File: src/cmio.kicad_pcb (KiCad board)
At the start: 2 copper layers, 78.7 x 29.2 mm, 37 parts, among them J1 USB_POWER, J3 BANK0, J4 USB_OTG, J5 CM3Lite, J6 TVOUT, J7 BANK1, J8 Micro_SD_Card_TFP09_2_12B, SW1 Reset, U1 AP3417B, U2 AP3417B, U3 SP6203EM5-L-2-8/TR, U4 AP2401

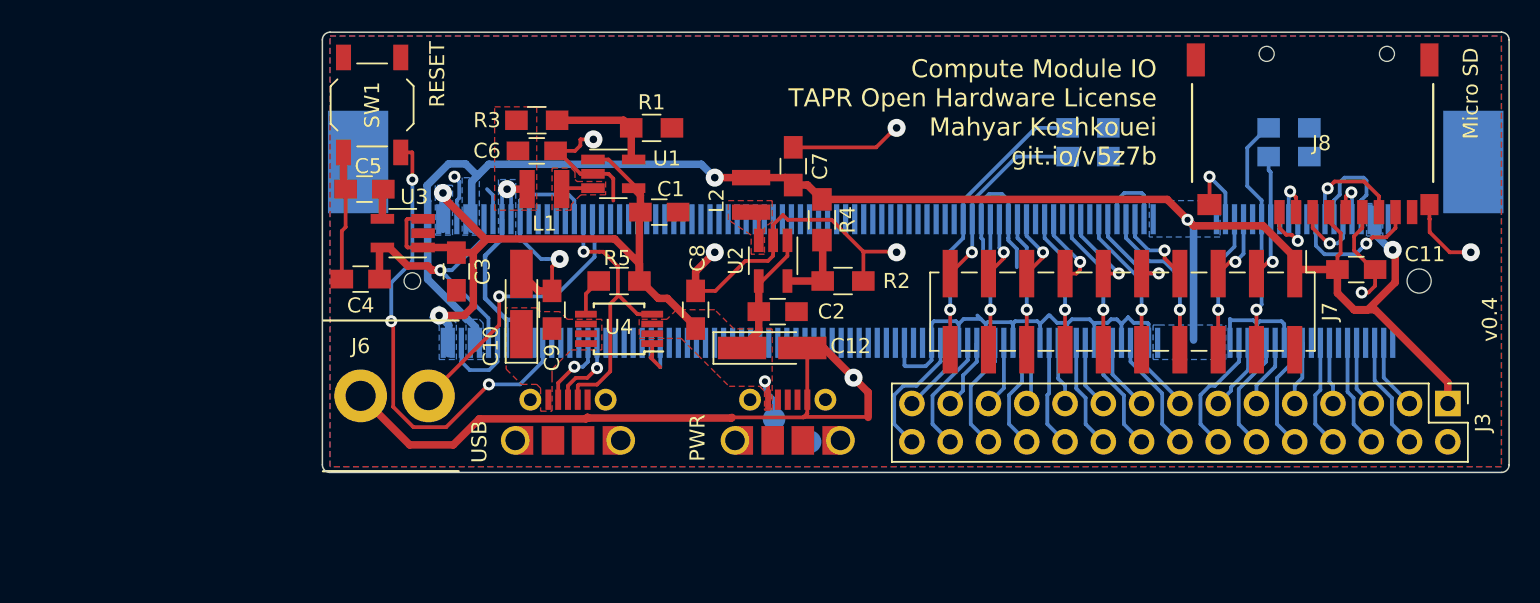
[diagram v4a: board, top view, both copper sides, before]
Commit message: Complete Routing
Signed-off-by: Mahyar Koshkouei <mahyar.koshkouei@gmail.com>
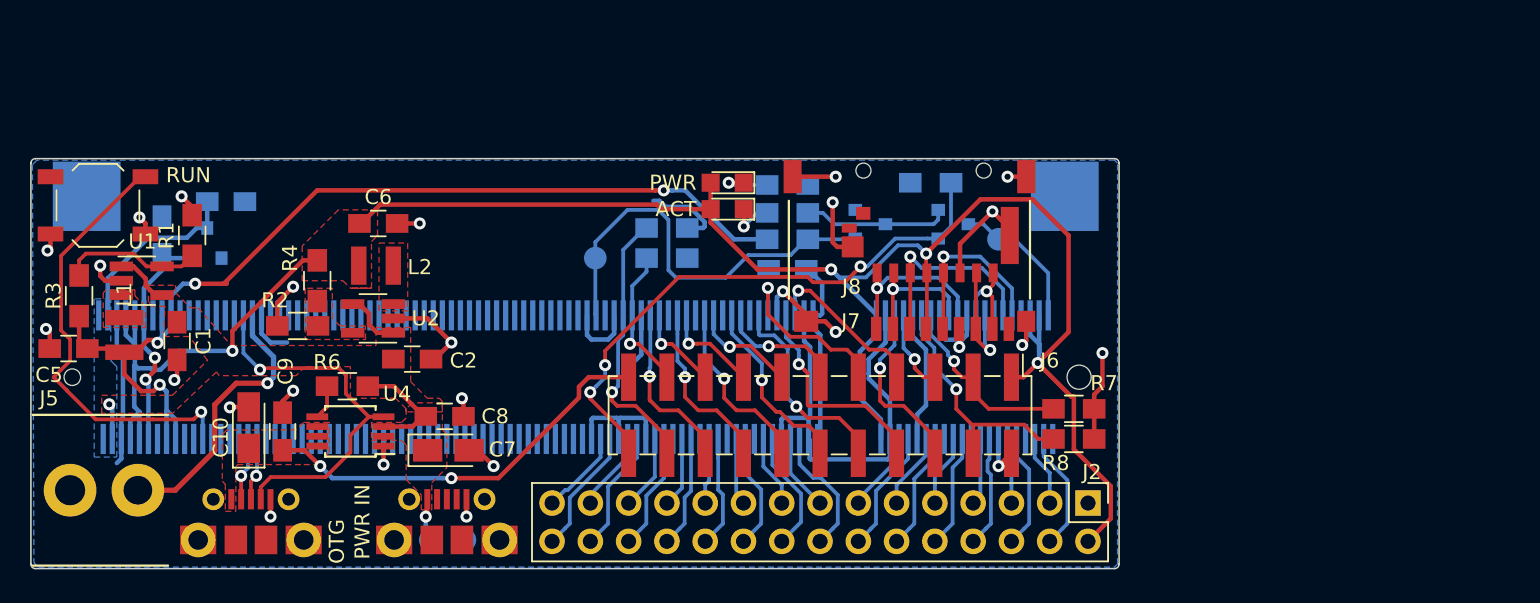
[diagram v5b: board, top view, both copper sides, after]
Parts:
- removed C12: 47uF, Capacitors_Tantalum_SMD:CP_Tantalum_Case-A_EIA-3216-18_Hand
- removed J1: USB_POWER, foot:Molex_Right_Angle_SMT_TypeB_MicroUSB_105017_CircularOnly
- removed J3: BANK0, Pin_Headers:Pin_Header_Straight_2x15_Pitch2.54mm
- removed SW1: Reset, Buttons_Switches_SMD:SW_SPST_TL3342
- added ACT: STATUS LED, LEDs:LED_0805, F.Cu at (131.0, 91.8)
- added J2: BANK0, Pin_Headers:Pin_Header_Straight_2x15_Pitch2.54mm, F.Cu at (154.9, 111.3)
- added OTG: USB_OTG, foot:Molex_Right_Angle_SMT_TypeB_MicroUSB_105017_CircularOnly_annular_fix, F.Cu at (99.4, 111.0)
- added PWR: PWR LED, LEDs:LED_0805, F.Cu at (131.0, 90.0)
- added PWR IN: USB_POWER, foot:Molex_Right_Angle_SMT_TypeB_MicroUSB_105017_CircularOnly_annular_fix, F.Cu at (112.4, 111.0)
- added Q1: 2N7002, TO_SOT_Packages_SMD:SOT-23, B.Cu at (146.0, 92.8)
- added Q2: 2N7002, TO_SOT_Packages_SMD:SOT-23, B.Cu at (140.5, 92.8)
- added R10: 100k, Resistors_SMD:R_0805_HandSoldering, B.Cu at (127.0, 93.0)
- added R11: 100k, Resistors_SMD:R_0805_HandSoldering, B.Cu at (135.0, 93.8)
- added R12: 100k, Resistors_SMD:R_0805_HandSoldering, B.Cu at (144.5, 90.0)
- added R13: 470R, Resistors_SMD:R_0805_HandSoldering, B.Cu at (135.0, 92.0)
- added RUN: Reset, Buttons_Switches_SMD:SW_SPST_TL3342, F.Cu at (89.2, 91.5)
- added TP3: TEST, Measurement_Points:Measurement_Point_Round-SMD-Pad_Small, B.Cu at (149.0, 93.8)
- added TP4: TEST, Measurement_Points:Measurement_Point_Round-SMD-Pad_Small, B.Cu at (122.2, 95.0)
- C10: footprint Capacitors_Tantalum_SMD:CP_Tantalum_Case-A_EIA-3216-18_Hand -> Capacitors_Tantalum_SMD:CP_Tantalum_Case-A_EIA-3216-18_Reflow
- C11: value 0.1uF -> 4.7uF; moved to B.Cu
- C3, C4: value 4.7uF -> 1uF; moved to B.Cu
- C5: value 10nF -> 4.7uF
- C7: value 4.7uF -> 47uF; footprint Capacitors_SMD:C_0805_HandSoldering -> Capacitors_Tantalum_SMD:CP_Tantalum_Case-A_EIA-3216-18_Reflow
- J4: value USB_OTG -> CM3Lite; footprint foot:Molex_Right_Angle_SMT_TypeB_MicroUSB_105017_CircularOnly -> foot:CM3_Socket_SODIMM_DDR1-2_TE_1473149_4_NoHole_NoEndSilkS; moved to B.Cu
- J5: value CM3Lite -> TVOUT; footprint foot:CM3_Socket_SODIMM_DDR1-2_TE_1612618_NoHole_NoEndSilkS -> foot:RCA_PHONO; moved to F.Cu
- J6: value TVOUT -> Conn_02x11_Odd_Even; footprint foot:RCA_PHONO -> Pin_Headers:Pin_Header_Straight_2x11_Pitch2.54mm_SMD
- J7: value BANK1 -> Micro_SD_Card_TFP09_2_12B; footprint Pin_Headers:Pin_Header_Straight_2x10_Pitch2.54mm_SMD -> foot:TFP09-2-12B
- J8: value Micro_SD_Card_TFP09_2_12B -> Micro_SD_Card_Molex_47219-2001; footprint foot:TFP09-2-12B -> foot:Molex_Micro_SD_47309-3751
- R5: value 10K -> 470R; moved to B.Cu
- R6: value 100K -> 10k; moved to F.Cu
- R7, R8: value 100K -> 100k; moved to F.Cu
- R9: value 100K -> 100k
- U3: value SP6203EM5-L-2-8/TR -> AP2138; footprint TO_SOT_Packages_SMD:SOT-23-5_HandSoldering -> TO_SOT_Packages_SMD:SOT-23; moved to B.Cu
- moved R6 64.3 mm to (105.8, 103.5), turned to 180 degrees
- moved J5 57.8 mm to (87.4, 110.4), turned to 0 degrees
- moved C11 37.7 mm to (135.0, 95.8), turned to 180 degrees
- moved R2 36.3 mm to (102.5, 99.5), turned to 180 degrees
- moved R4 33.7 mm to (103.8, 96.5)
- moved C1 33.1 mm to (94.5, 100.5), turned to 270 degrees
- moved J4 32.9 mm to (87.5, 102.9), turned to 180 degrees
- moved R3 32.5 mm to (88.0, 97.5), turned to 90 degrees
- moved U1 32.1 mm to (92.2, 96.5)
- moved R1 31.3 mm to (95.5, 93.5), turned to 90 degrees
- moved J6 30.5 mm to (137.2, 105.4), turned to 270 degrees
- moved C7 29.6 mm to (112.5, 107.8), turned to 0 degrees
- moved L1 29.5 mm to (91.0, 100.1), turned to 270 degrees
- moved R9 29.2 mm to (127.0, 95.0)
- moved U2 26.8 mm to (107.5, 99.0), turned to 180 degrees
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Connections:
- C10 pad 1: Net-(C10-Pad1) -> VBUS
- C4 pad 1: +2V8 -> +2V5
- C5 pad 1: GND -> +1V8
- C5 pad 2: Net-(C5-Pad2) -> GND
- C6 pad 1: +1V8 -> +3V3
- C7 pad 1: +3V3 -> +5V
- C9 pad 1: Net-(C10-Pad1) -> VBUS
- J4 pad 1: Net-(C10-Pad1) -> GND
- J4 pad 2: /D- -> EMMC_DISABLE_N
- J4 pad 3: /D+ -> /BCM_0
- J4 pad 4: OTGID -> +3V3
- J4 pad 5: GND -> /BCM_1
- J5 pad 1: GND -> /TV
- J5 pad 2: Net-(J5-Pad2) -> GND
- J6 pad 1: Net-(J5-Pad166) -> +3V3
- J7 pad 1: +3V3 -> DAT2
- J7 pad 10: /BCM_35 -> GND
- J7 pad 2: GND -> DAT3
- J7 pad 3: /BCM_28 -> CMD
- J7 pad 4: /BCM_29 -> +3V3
- J7 pad 5: /BCM_30 -> CLK
- J7 pad 6: /BCM_31 -> GND
- J7 pad 7: /BCM_32 -> DAT0
- J7 pad 8: /BCM_33 -> DAT1
- J7 pad 9: /BCM_34 -> Net-(J7-Pad9)
- J8 pad 9: Net-(J8-Pad9) -> GND
- R5 pad 1: +5V -> Net-(D1-Pad1)
- R5 pad 2: Net-(R5-Pad2) -> GND
- R6 pad 1: /BCM_28 -> +5V
- R6 pad 2: GND -> Net-(R6-Pad2)
- R7 pad 1: /BCM_29 -> /BCM_28
- R8 pad 1: /BCM_44 -> /BCM_29
- R9 pad 1: /BCM_45 -> /BCM_44
- U3 pad 1: +5V -> GND
- U3 pad 2: GND -> +2V5
- U4 pad 5: Net-(R5-Pad2) -> Net-(R6-Pad2)
- U4 pad 6: Net-(C10-Pad1) -> VBUS
- U4 pad 7: Net-(C10-Pad1) -> VBUS
- U4 pad 8: Net-(C10-Pad1) -> VBUS
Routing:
- net GND: track 210.0 -> 139.7 mm, vias 10 -> 26
- net +1V8: track 16.8 -> 67.5 mm, vias 1 -> 4
- net USB_SET: track 0.00 -> 37.8 mm, vias 0 -> 3
- net +3V3: track 115.3 -> 149.2 mm, vias 3 -> 4
- net +5V: track 64.7 -> 32.9 mm, vias 3 -> 2
- net Net-(J5-Pad177): track 31.8 -> 0.00 mm, vias 3 -> 0
- net /RESET: track 0.00 -> 29.5 mm, vias 0 -> 1
- net STATUS_LED: track 0.00 -> 27.9 mm
- net VBUS: track 0.00 -> 26.9 mm, vias 0 -> 2
- net /TV: track 0.00 -> 18.6 mm, vias 0 -> 1
- net Net-(J5-Pad166): track 18.5 -> 0.00 mm, vias 1 -> 0
- net +2V8: track 17.8 -> 0.00 mm, vias 1 -> 0
- net +2V5: track 0.00 -> 15.5 mm, vias 0 -> 2
- net Net-(Q1-Pad2): track 0.00 -> 9.73 mm
- net EMMC_DISABLE_N: track 0.00 -> 9.45 mm
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- added copper zone on F.Cu, net +3V3
- added copper zone on F.Cu, net Net-(R2-Pad1)
- added copper zone on F.Cu, net VBUS
- removed copper zone on B.Cu, net +1V8
- removed copper zone on F.Cu, net +1V8
- removed copper zone on B.Cu, net +3V3
- removed copper zone on F.Cu, net GND
- removed copper zone on F.Cu, net Net-(C10-Pad1)
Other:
- board size 78.7 x 29.2 mm -> 72.2 x 27.2 mm
- net class TV added: clearance 0.2, trace_width 0.35, via_dia 0.8, via_drill 0.4
- board text removed: "Compute Module IO TAPR Open Hardware License Mahyar Koshkouei git.io/v5z7b"
- board text removed: "Micro SD"
- board text removed: "PWR"
- board text removed: "RESET"
- board text removed: "Raspberry Pi Compute Module (1/3/3L)"
- board text removed: "USB"
- board text removed: "v0.4"
